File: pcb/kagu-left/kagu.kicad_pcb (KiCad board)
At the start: 2 copper layers, 127 x 91.5 mm, 62 parts, among them SW1 SW_Push, SW10 SW_Push, SW11 SW_Push, SW12 SW_Push, SW13 SW_Push, SW14 SW_Push, SW15 SW_Push, SW16 SW_Push, SW17 SW_Push, SW18 SW_Push, SW19 SW_Push, SW2 SW_Push, SW3 SW_Push, SW4 SW_Push, SW5 SW_Push, SW6 SW_Push, SW7 SW_Push, SW8 SW_Push, SW9 SW_Push, U1 XIAO-nRF52840-Plus-SMD

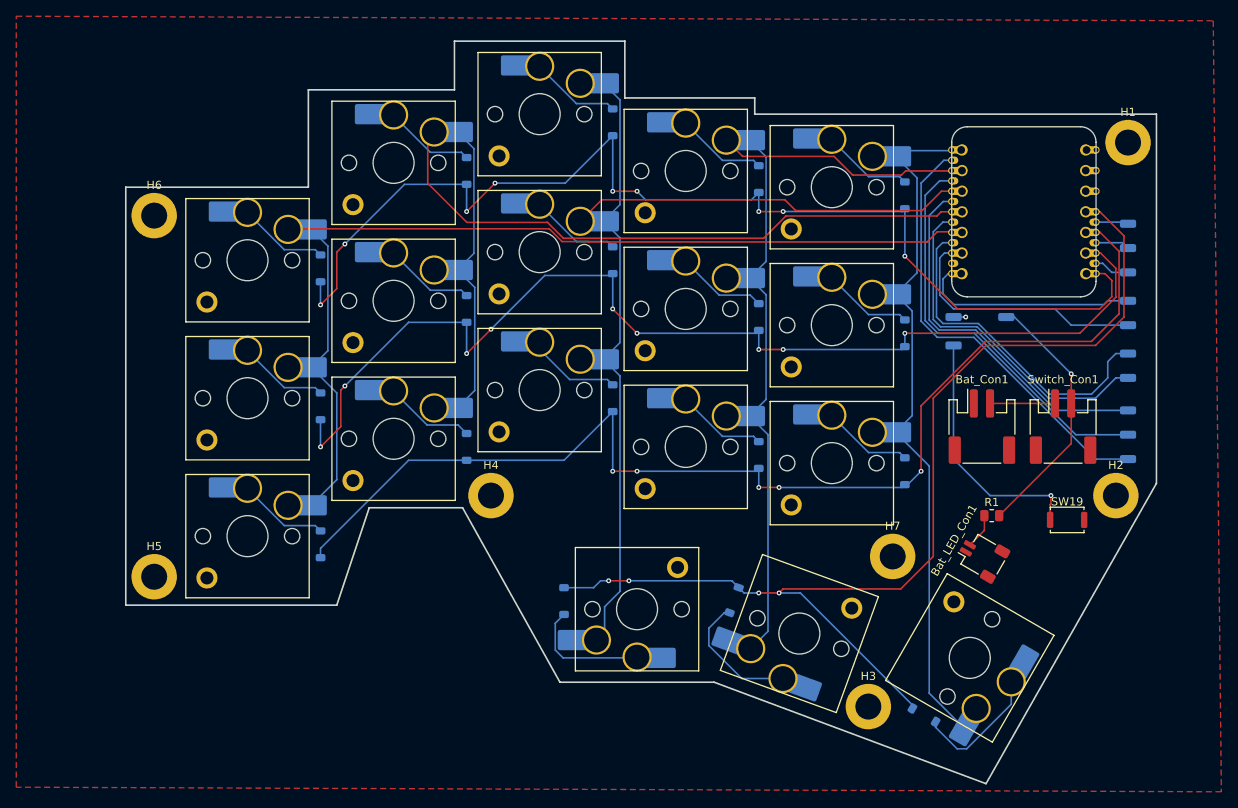
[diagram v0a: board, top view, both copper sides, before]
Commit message: feat(pcb): match both sides
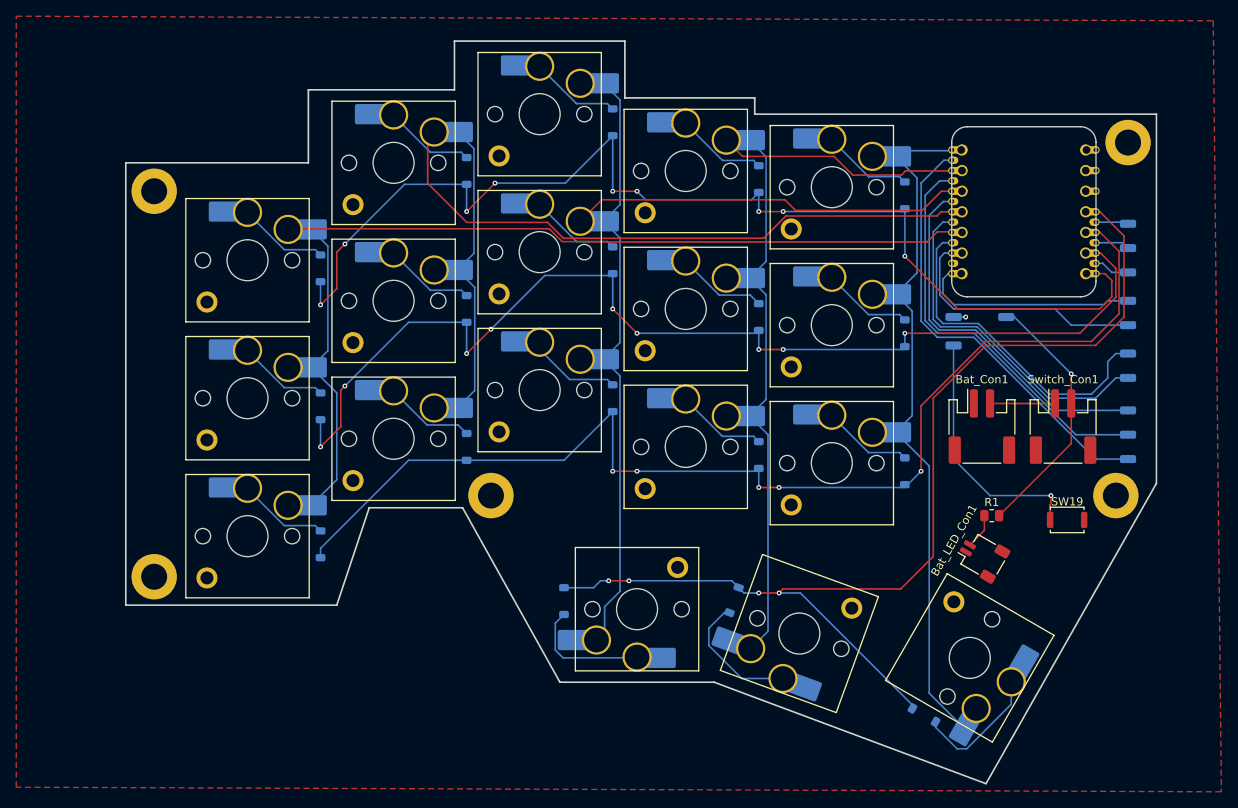
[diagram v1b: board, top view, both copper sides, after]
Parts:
- removed H3, H7: MountingHole, MountingHole:MountingHole_3.2mm_M3_DIN965_Pad
- moved H6 3.00 mm to (74.5, 61.5)
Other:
- outline, holes or cut-outs redrawn
